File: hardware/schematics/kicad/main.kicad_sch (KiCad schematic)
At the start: 297 parts, among them IC1 74377N, IC10 74153N, IC100 74273N, IC101 74273N, IC102 74273N, IC103 74273N, IC104 74273N, IC105 74273N, IC106 74273N, IC107 74273N, IC108 74273N, IC109 7427N, IC11 74257N, IC110 74245N, IC111 74257N, IC112 74257N, IC113 7404N, IC114 74377N, IC115 74244N, IC116 74138N, IC117 74244N, IC118 74244N, IC119 74244N, IC12 74257N, IC120 74244N, IC121 7404N, IC122 7420N, IC123 74151N, IC124 74151N, IC125 74151N, IC126 74151N, IC127 74151N, IC128 74151N, IC129 74151N, IC13 7408N, IC130 74151N, IC131 74151N, IC132 74151N, IC133 74151N, IC134 74151N, IC135 74151N, IC136 74151N, IC137 74151N, IC138 74151N, IC139 74151N, IC14 74153N, IC140 74151N, IC141 74151N, IC142 74151N, IC143 74151N, IC144 74151N, IC145 74151N, IC146 74151N, IC147 74151N, IC148 74151N, IC149 74151N, IC15 74257N, IC150 74151N, IC151 74151N, IC152 74151N, IC153 74151N, IC154 74151N, IC155 74257N, IC156 74257N, IC157 74257N, IC158 74257N, IC159 74257N, IC16 74257N, IC160 74257N, IC161 7408N, IC162 7430N, IC163 7404N, IC164 7474N, IC165 7427N, IC166 74153N, IC167 74153N, IC168 74153N, IC169 74153N, IC17 74153N, IC170 7474N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

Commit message: floppy drive kernel code
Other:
- note added: "this 244 needs to be a flip flop instead, because the DRQ and READY lines are actually asynchronous."

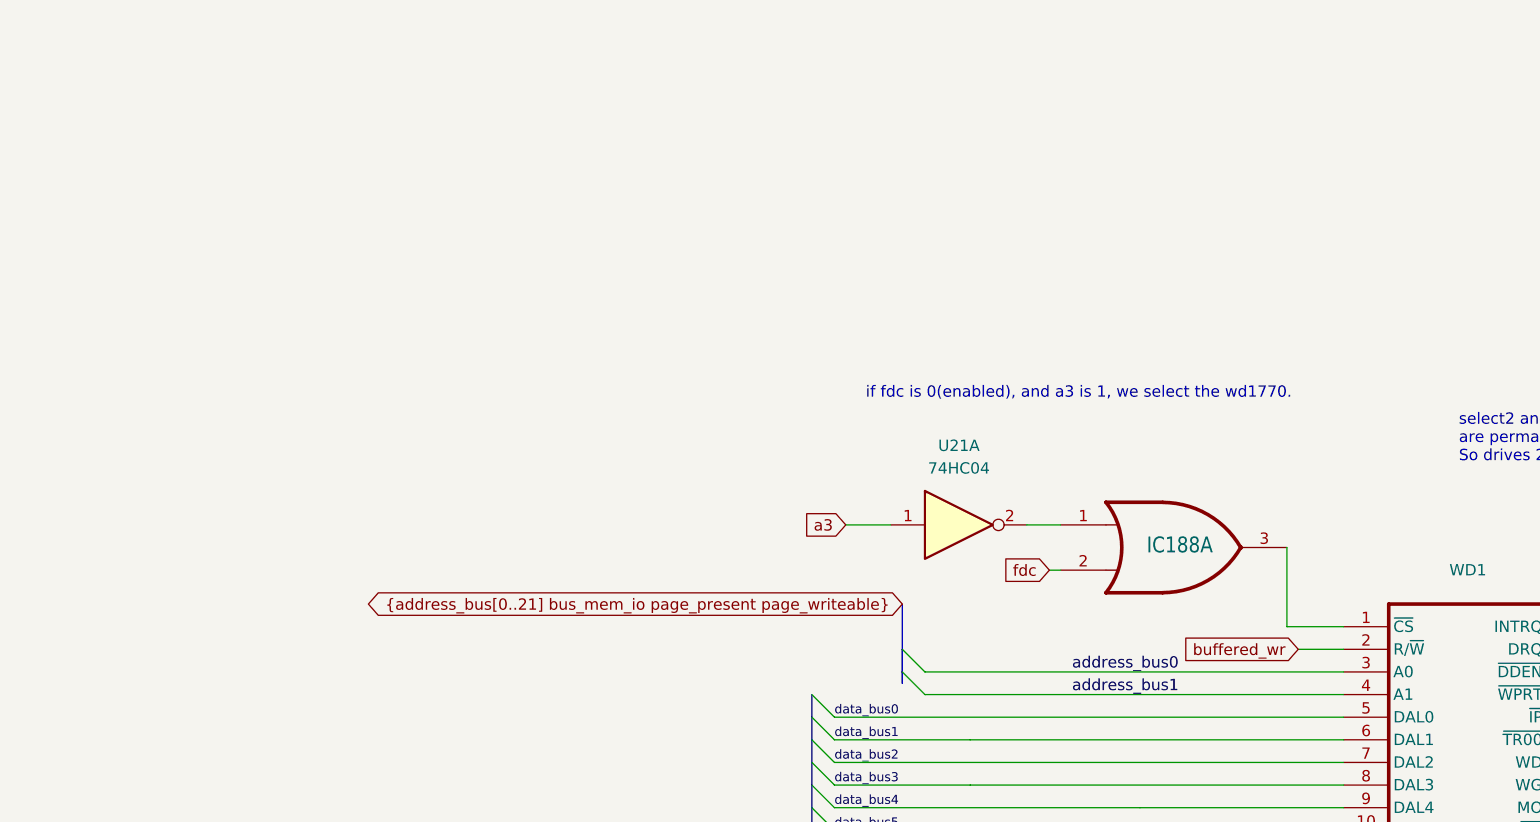
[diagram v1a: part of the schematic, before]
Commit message: various fixed for floppy disk driver - working now
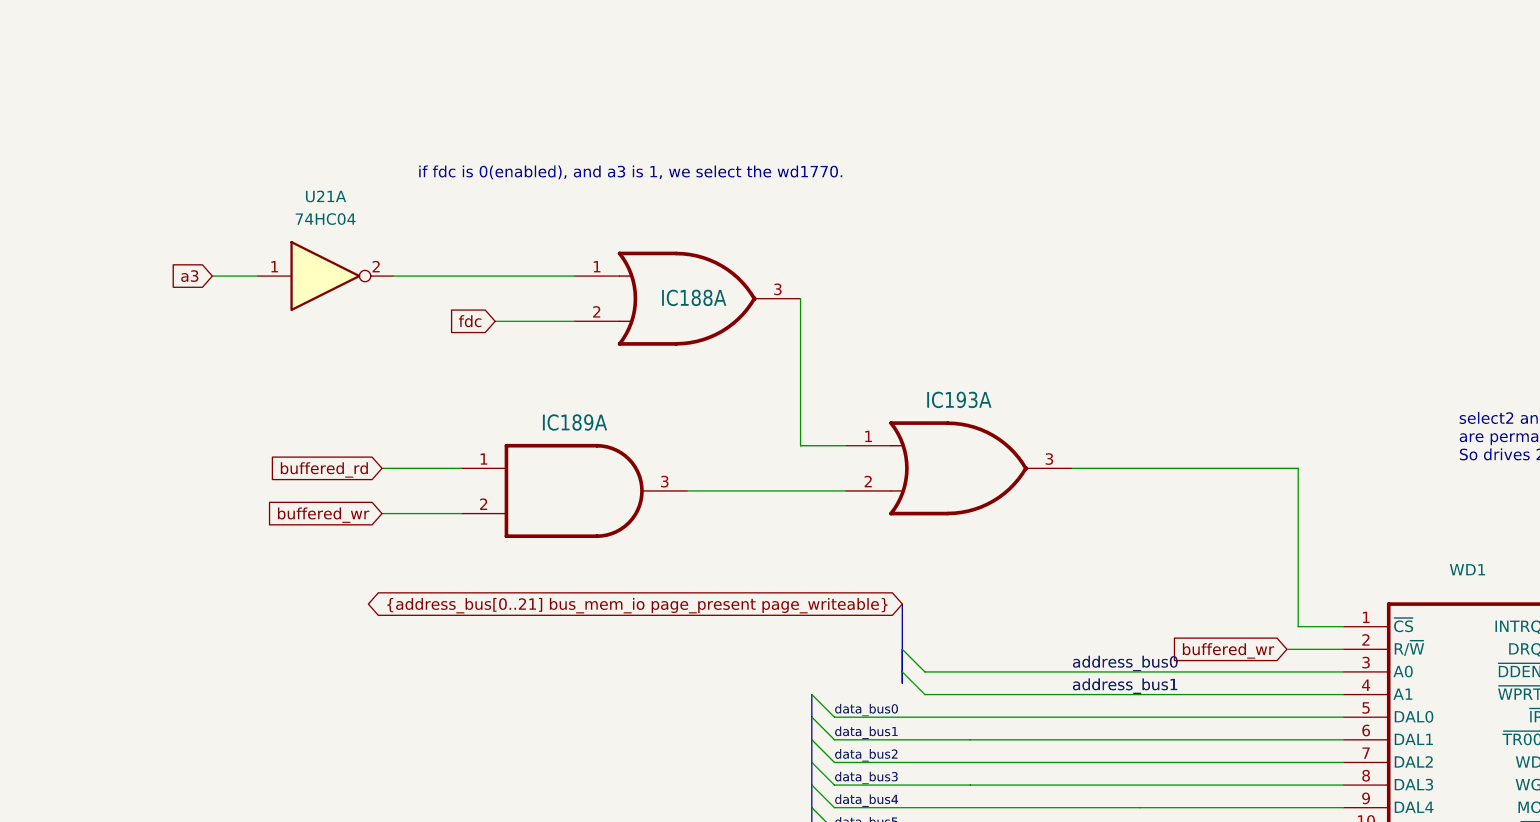
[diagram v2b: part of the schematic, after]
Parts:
- added IC189: ~, main:DIL14, symbol main-eagle-import:7408N
- added IC193: ~, main:DIL14, symbol main-eagle-import:7432N
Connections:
- net buffered_rd: now also IC189.1 (I0)
- net buffered_wr: now also IC189.2 (I1)
- net at WD1.1 (~{CS}): now also IC193.3 (O); no longer IC188.3 (O)
- new net: IC189.3 (O), IC193.2 (I1)
- new net: IC188.3 (O), IC193.1 (I0)
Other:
- moved on the sheet: IC188A, U21A

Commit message: cleanup
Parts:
- added IC199: 74138N, Package_DIP:DIP-16_W7.62mm, symbol main-eagle-import:74138N
- added IC201: ~, main:DIL14, symbol main-eagle-import:7404N
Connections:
- net GND: now also IC199.2 (B), IC199.3 (C), IC199.4 (G2A), IC199.5 (G2B)
- net uart_0_en: now also IC199.15 (Y0); no longer IC116.15 (Y0)
- net uart_1_en: now also IC199.14 (Y1); no longer IC116.14 (Y1)
- net at BIOS_ROM1.7 (A3), IC172.12 (Y4), U15.7 (A3): now also IC199.1 (A)
- new net: IC116.15 (Y0), IC201.1 (I)
- new net: IC199.6 (G1), IC201.2 (O)
